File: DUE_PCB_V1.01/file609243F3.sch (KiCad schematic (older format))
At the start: 38 parts, among them J29 Motor Left, J30 Cutter Motor, J31 Motor Right, J32 Motor_Right1, J33 Motor_Right2, J34 Motor_Left1, J35 Motor_Left2, J36 Cutter_Motor, J37 ODORight1, J38 ODORight2, J39 ODOLeft1, J40 ODOLeft2, J41 ODOCutter

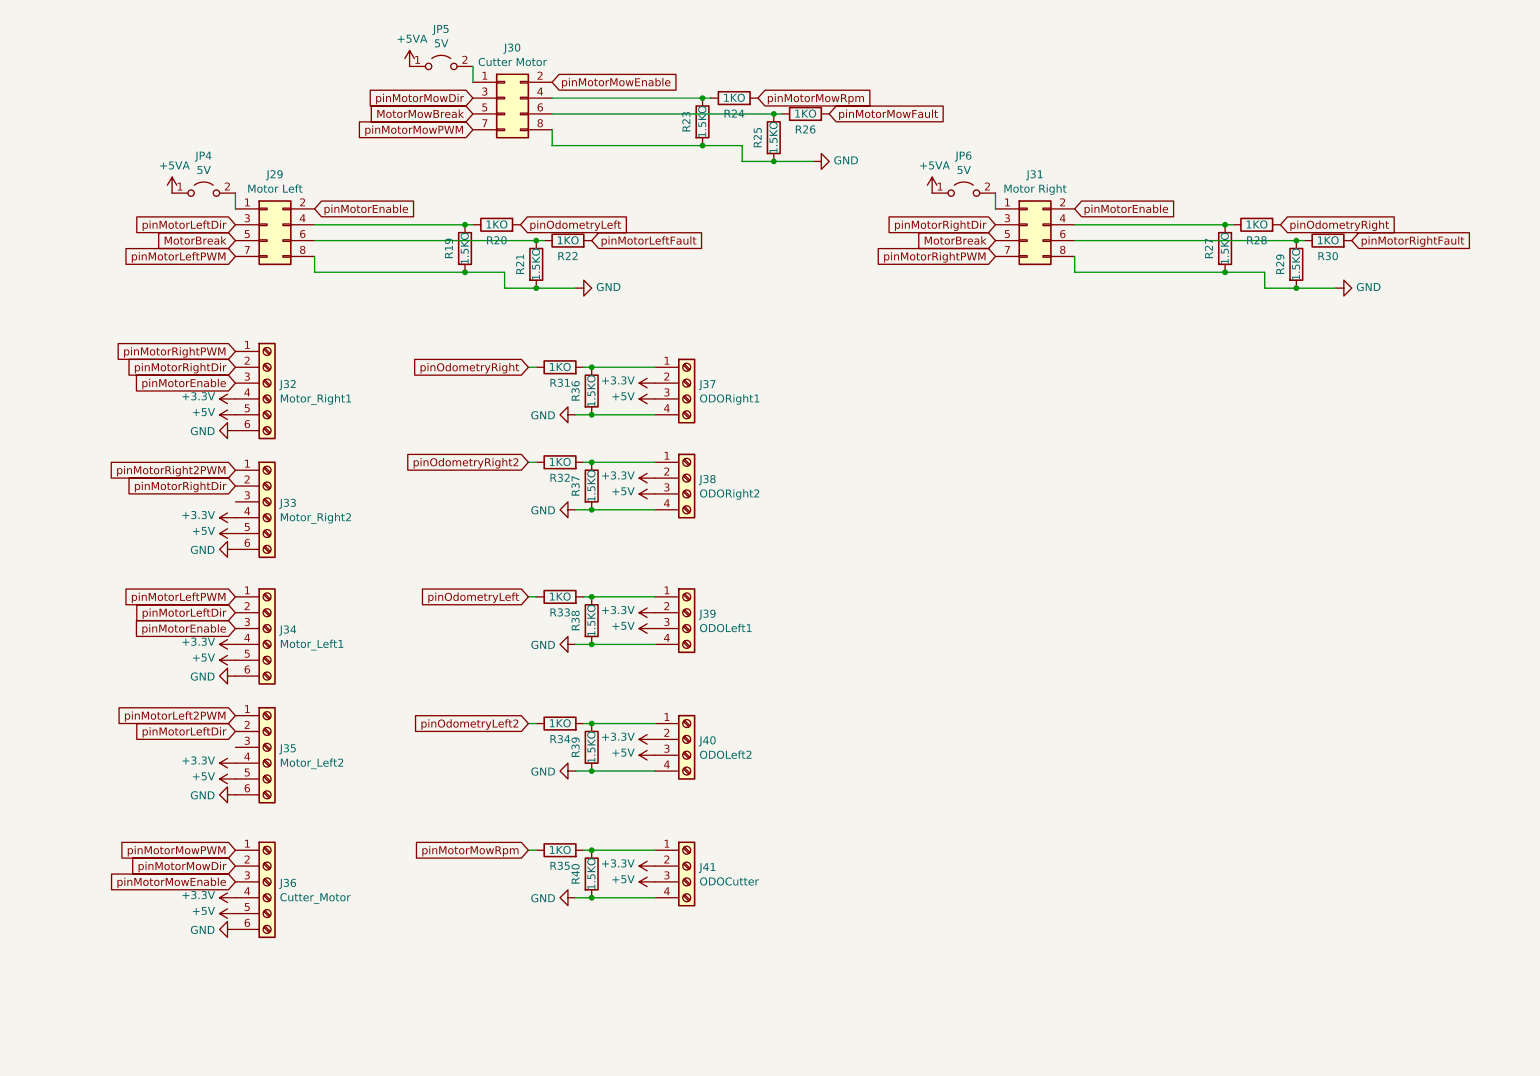
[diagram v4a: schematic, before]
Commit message: Add new Motor Schematic
Add new Motor Schematic
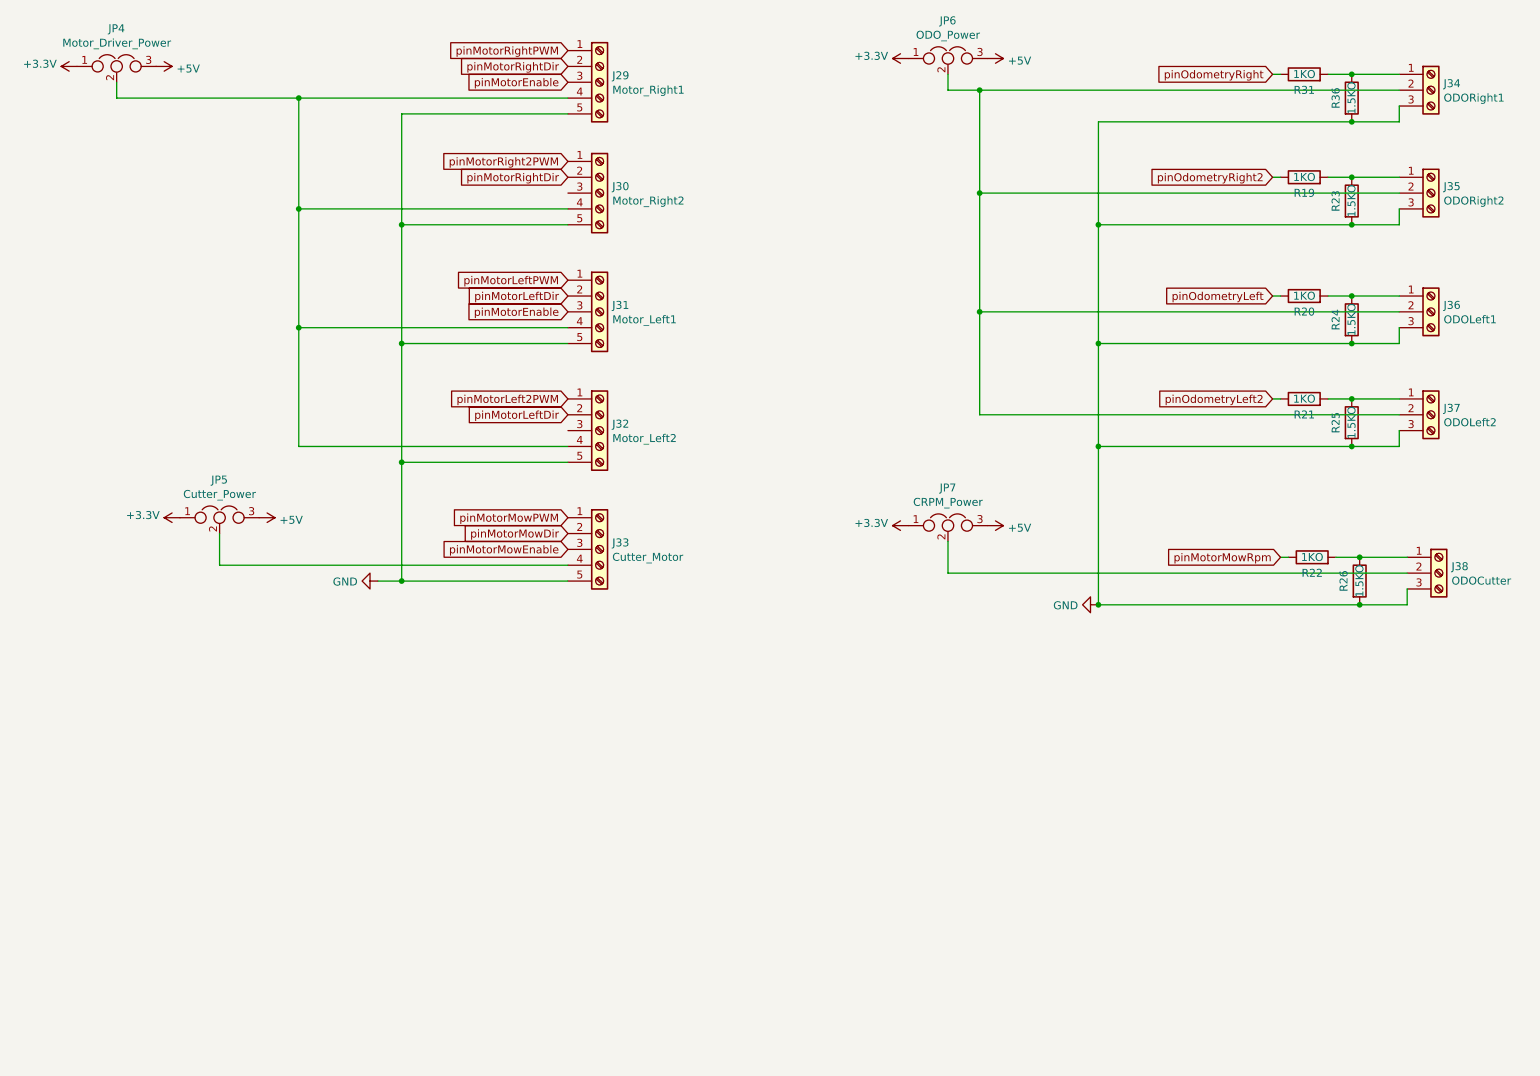
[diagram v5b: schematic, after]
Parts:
- removed J29: Motor Left, Connector_PinSocket_2.54mm:PinSocket_2x04_P2.54mm_Vertical, symbol Connector_Generic:Conn_02x04_Odd_Even
- removed J30: Cutter Motor, Connector_PinSocket_2.54mm:PinSocket_2x04_P2.54mm_Vertical, symbol Connector_Generic:Conn_02x04_Odd_Even
- removed J31: Motor Right, Connector_PinSocket_2.54mm:PinSocket_2x04_P2.54mm_Vertical, symbol Connector_Generic:Conn_02x04_Odd_Even
- removed J32: Motor_Right1, Connector_PinHeader_2.54mm:PinHeader_1x06_P2.54mm_Vertical, symbol Connector:Screw_Terminal_01x06
- removed J33: Motor_Right2, Connector_PinHeader_2.54mm:PinHeader_1x06_P2.54mm_Vertical, symbol Connector:Screw_Terminal_01x06
- removed J34: Motor_Left1, Connector_PinHeader_2.54mm:PinHeader_1x06_P2.54mm_Vertical, symbol Connector:Screw_Terminal_01x06
- removed J35: Motor_Left2, Connector_PinHeader_2.54mm:PinHeader_1x06_P2.54mm_Vertical, symbol Connector:Screw_Terminal_01x06
- removed J36: Cutter_Motor, Connector_PinHeader_2.54mm:PinHeader_1x06_P2.54mm_Vertical, symbol Connector:Screw_Terminal_01x06
- removed J37: ODORight1, Connector_PinHeader_2.54mm:PinHeader_1x04_P2.54mm_Vertical, symbol Connector:Screw_Terminal_01x04
- removed J38: ODORight2, Connector_PinHeader_2.54mm:PinHeader_1x04_P2.54mm_Vertical, symbol Connector:Screw_Terminal_01x04
- removed J39: ODOLeft1, Connector_PinHeader_2.54mm:PinHeader_1x04_P2.54mm_Vertical, symbol Connector:Screw_Terminal_01x04
- removed J40: ODOLeft2, Connector_PinHeader_2.54mm:PinHeader_1x04_P2.54mm_Vertical, symbol Connector:Screw_Terminal_01x04
- removed J41: ODOCutter, Connector_PinHeader_2.54mm:PinHeader_1x04_P2.54mm_Vertical, symbol Connector:Screw_Terminal_01x04
- removed JP4, JP5, JP6: 5V, Connector_PinSocket_2.54mm:PinSocket_1x02_P2.54mm_Vertical, symbol Jumper:Jumper_2_Open
- removed R27, R29, R37, R38, R39, R40: 1.5KO, Resistor_THT:R_Axial_DIN0207_L6.3mm_D2.5mm_P2.54mm_Vertical, symbol Device:R
- removed R28, R30, R32, R33, R34, R35: 1KO, Resistor_THT:R_Axial_DIN0207_L6.3mm_D2.5mm_P2.54mm_Vertical, symbol Device:R
- added J29: Motor_Right1, Connector_JST:JST_XH_B5B-XH-A_1x05_P2.50mm_Vertical, symbol Connector:Screw_Terminal_01x05
- added J30: Motor_Right2, Connector_JST:JST_XH_B5B-XH-A_1x05_P2.50mm_Vertical, symbol Connector:Screw_Terminal_01x05
- added J31: Motor_Left1, Connector_JST:JST_XH_B5B-XH-A_1x05_P2.50mm_Vertical, symbol Connector:Screw_Terminal_01x05
- added J32: Motor_Left2, Connector_JST:JST_XH_B5B-XH-A_1x05_P2.50mm_Vertical, symbol Connector:Screw_Terminal_01x05
- added J33: Cutter_Motor, Connector_JST:JST_XH_B5B-XH-A_1x05_P2.50mm_Vertical, symbol Connector:Screw_Terminal_01x05
- added J34: ODORight1, Connector_JST:JST_XH_B3B-XH-A_1x03_P2.50mm_Vertical, symbol Connector:Screw_Terminal_01x03
- added J35: ODORight2, Connector_JST:JST_XH_B3B-XH-A_1x03_P2.50mm_Vertical, symbol Connector:Screw_Terminal_01x03
- added J36: ODOLeft1, Connector_JST:JST_XH_B3B-XH-A_1x03_P2.50mm_Vertical, symbol Connector:Screw_Terminal_01x03
- added J37: ODOLeft2, Connector_JST:JST_XH_B3B-XH-A_1x03_P2.50mm_Vertical, symbol Connector:Screw_Terminal_01x03
- added J38: ODOCutter, Connector_JST:JST_XH_B3B-XH-A_1x03_P2.50mm_Vertical, symbol Connector:Screw_Terminal_01x03
- added JP4: Motor_Driver_Power, Connector_PinHeader_2.54mm:PinHeader_1x03_P2.54mm_Vertical, symbol Device:Jumper_NC_Dual
- added JP5: Cutter_Power, Connector_PinHeader_2.54mm:PinHeader_1x03_P2.54mm_Vertical, symbol Device:Jumper_NC_Dual
- added JP6: ODO_Power, Connector_PinHeader_2.54mm:PinHeader_1x03_P2.54mm_Vertical, symbol Device:Jumper_NC_Dual
- added JP7: CRPM_Power, Connector_PinHeader_2.54mm:PinHeader_1x03_P2.54mm_Vertical, symbol Device:Jumper_NC_Dual
- R19, R21: value 1.5KO -> 1KO
- R24, R26: value 1KO -> 1.5KO
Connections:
- net pinMotorMowFault is gone; now on net GND: R26.2
- net +3V3: now also JP4.1, JP5.1, JP6.1, JP7.1
- net +5V: now also JP4.3, JP5.3, JP6.3, JP7.3
- net GND: now also R24.2, J29.5 (Pin_5), J30.5 (Pin_5), J31.5 (Pin_5), J32.5 (Pin_5), J33.5 (Pin_5), J34.3 (Pin_3), J35.3 (Pin_3), J36.3 (Pin_3), J37.3 (Pin_3), J38.3 (Pin_3); no longer R19.2, R21.2
- net pinMotorEnable: now also J29.3 (Pin_3), J31.3 (Pin_3)
- net pinMotorLeft2PWM: now also J32.1 (Pin_1)
- net pinMotorLeftDir: now also J31.2 (Pin_2), J32.2 (Pin_2)
- net pinMotorLeftPWM: now also J31.1 (Pin_1)
- net pinMotorMowDir: now also J33.2 (Pin_2)
- net pinMotorMowEnable: now also J33.3 (Pin_3)
- net pinMotorMowPWM: now also J33.1 (Pin_1)
- net pinMotorMowRpm: now also R22.1; no longer R24.2
- net pinMotorRight2PWM: now also J30.1 (Pin_1)
- net pinMotorRightDir: now also J29.2 (Pin_2), J30.2 (Pin_2)
- net pinMotorRightPWM: now also J29.1 (Pin_1)
- net pinOdometryLeft: now also R20.1; no longer R20.2
- net pinOdometryLeft2: now also R21.1
- net pinOdometryRight2: now also R19.1
- net at R25.1: now also R21.2, J37.1 (Pin_1); no longer R26.1
- net at R23.1: now also R19.2, J35.1 (Pin_1); no longer R24.1
- net at R31.2, R36.1: now also J34.1 (Pin_1)
- net pinMotorLeftFault: no longer names the net of R22.2
- net pinMotorLeftFault: now also R26.1, J38.1 (Pin_1)
- new net: J34.2 (Pin_2), J35.2 (Pin_2), J36.2 (Pin_2), J37.2 (Pin_2), JP6.2
- new net: J36.1 (Pin_1), R20.2, R24.1
- new net: J38.2 (Pin_2), JP7.2
- new net: J29.4 (Pin_4), J30.4 (Pin_4), J31.4 (Pin_4), J32.4 (Pin_4), JP4.2
- new net: J33.4 (Pin_4), JP5.2
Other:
- moved on the sheet: R31, R36

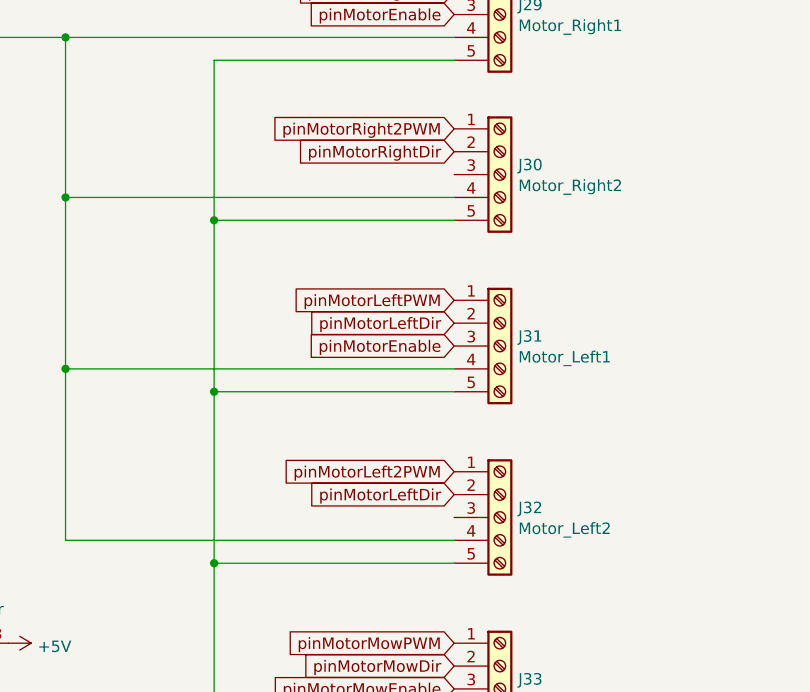
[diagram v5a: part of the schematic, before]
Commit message: Remove Lawn Sense Pins
Remove Lawn Sense Pins and add pinMotorLeft2Dir and pinMotorRight2Dir
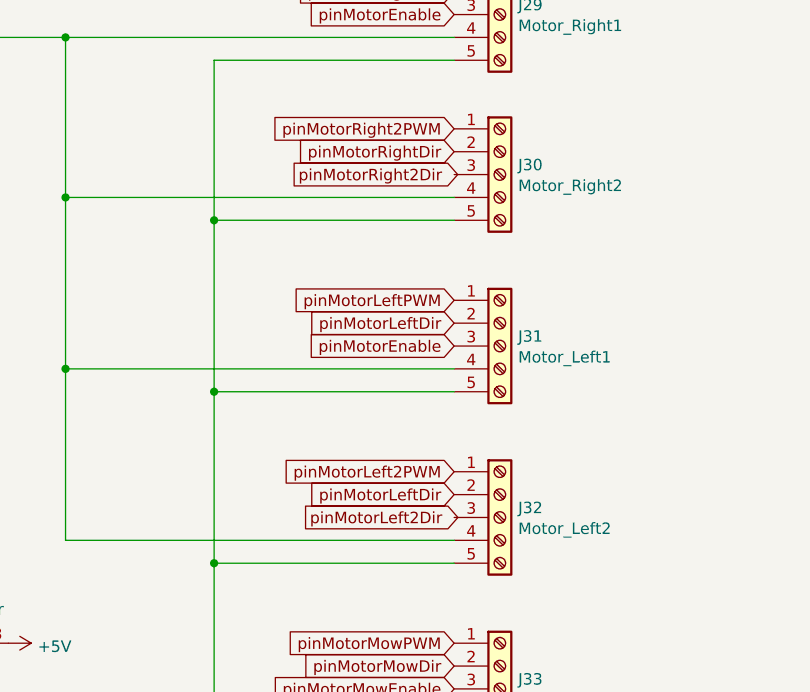
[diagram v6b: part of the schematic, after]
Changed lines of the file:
@@
 Wire Wire Line
 	4150 1300 3100 1300
-Connection ~ 3100 4250
-Wire Wire Line
-	3100 4250 4150 4250
 Wire Wire Line
 	4150 3500 3100 3500
@@
 Wire Wire Line
 	3100 3500 3100 4250
-Wire Wire Line
-	4150 2750 3100 2750
 Connection ~ 3100 2750
 Wire Wire Line
@@
 Wire Wire Line
 	1950 3950 1950 4150
-Wire Wire Line
-	1950 4150 4150 4150
 $Comp
 L Device:Jumper_NC_Dual JP4
@@
 	2450 3400 4150 3400
 Connection ~ 2450 1900
-Wire Wire Line
-	4150 2650 2450 2650
 Connection ~ 2450 2650
 Wire Wire Line
 	2450 2650 2450 3400
+Text GLabel 3450 1800 2    50   Output ~ 0
+pinMotorRight2Dir
+Connection ~ 3100 4250
+Wire Wire Line
+	4150 2750 3100 2750
+Wire Wire Line
+	4150 2650 2450 2650
+Text GLabel 3500 3300 2    50   Output ~ 0
+pinMotorLeft2Dir
+Wire Wire Line
+	1950 4150 4150 4150
+Wire Wire Line
+	3100 4250 4150 4250
 $EndSCHEMATC

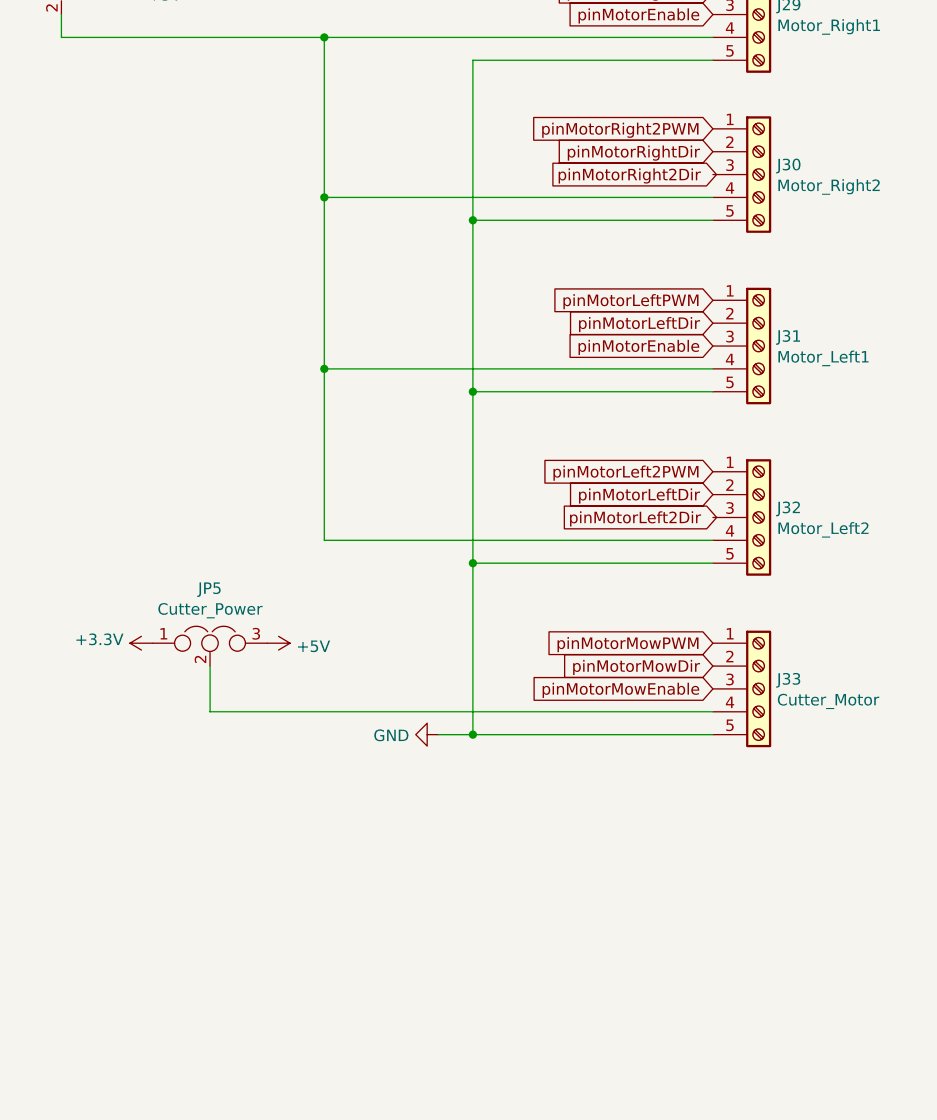
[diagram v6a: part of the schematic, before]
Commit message: Motor Connector correctly named
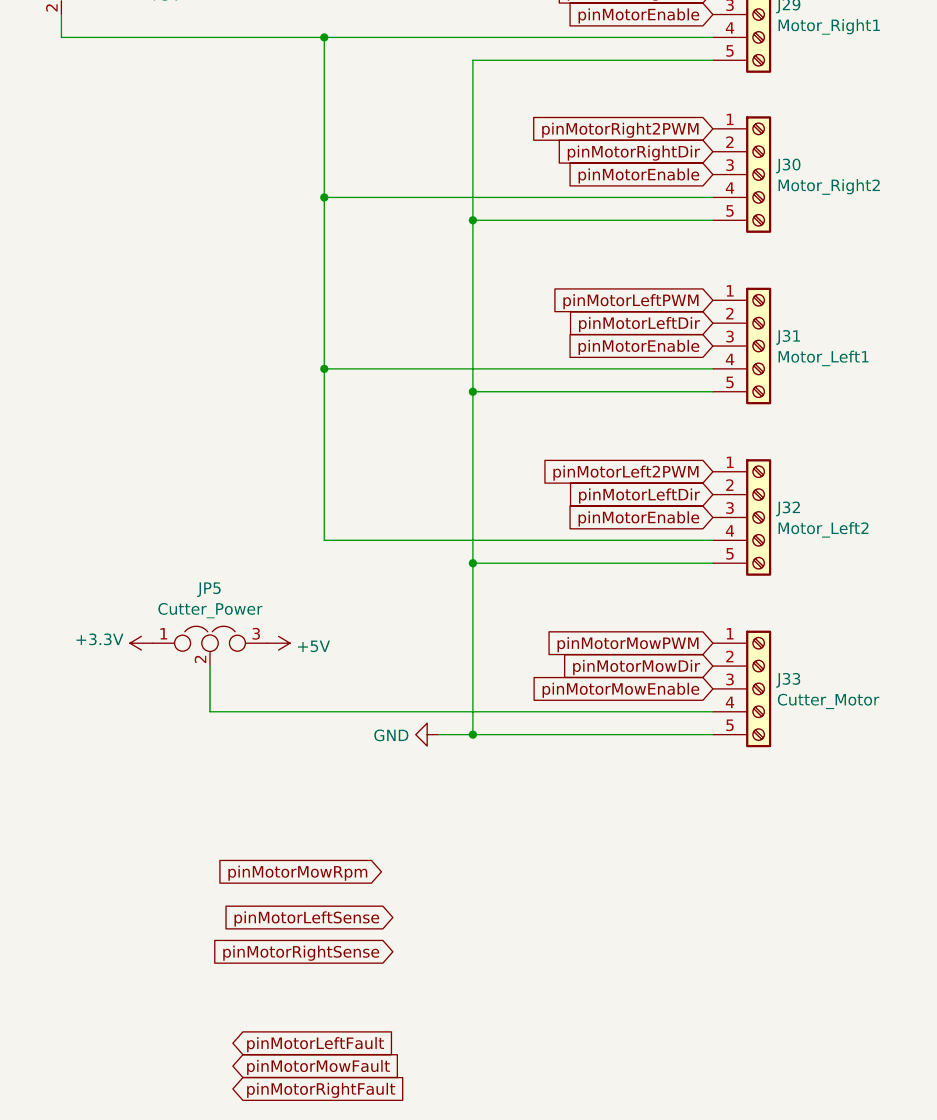
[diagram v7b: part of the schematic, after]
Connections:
- net pinMotorEnable: now also J30.3 (Pin_3), J32.3 (Pin_3)
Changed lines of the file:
@@
 Text GLabel 4150 2450 0    50   Input ~ 0
 pinMotorLeftDir
-Text GLabel 4150 2550 0    50   Input ~ 0
-pinMotorEnable
 Text GLabel 4150 3850 0    50   Input ~ 0
 pinMotorMowPWM
@@
 Wire Wire Line
 	2450 2650 2450 3400
-Text GLabel 3450 1800 2    50   Output ~ 0
-pinMotorRight2Dir
 Connection ~ 3100 4250
 Wire Wire Line
@@
 Wire Wire Line
 	4150 2650 2450 2650
-Text GLabel 3500 3300 2    50   Output ~ 0
-pinMotorLeft2Dir
 Wire Wire Line
 	1950 4150 4150 4150
 Wire Wire Line
 	3100 4250 4150 4250
+Text GLabel 2750 5050 0    50   Input ~ 0
+pinMotorLeftSense
+Text GLabel 2750 5200 0    50   Input ~ 0
+pinMotorRightSense
+Text GLabel 2050 5800 2    50   Input ~ 0
+pinMotorRightFault
+Text GLabel 2050 5600 2    50   Input ~ 0
+pinMotorLeftFault
+Text GLabel 2050 5700 2    50   Input ~ 0
+pinMotorMowFault
+Text GLabel 2700 4850 0    50   Input ~ 0
+pinMotorMowRpm
+Text GLabel 4150 1800 0    50   Input ~ 0
+pinMotorEnable
+Text GLabel 4150 2550 0    50   Input ~ 0
+pinMotorEnable
+Text GLabel 4150 3300 0    50   Input ~ 0
+pinMotorEnable
 $EndSCHEMATC
